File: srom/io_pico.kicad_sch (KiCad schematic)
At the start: 2 parts, among them J201 Conn_01x03_Female, U201 Pico-2 IO

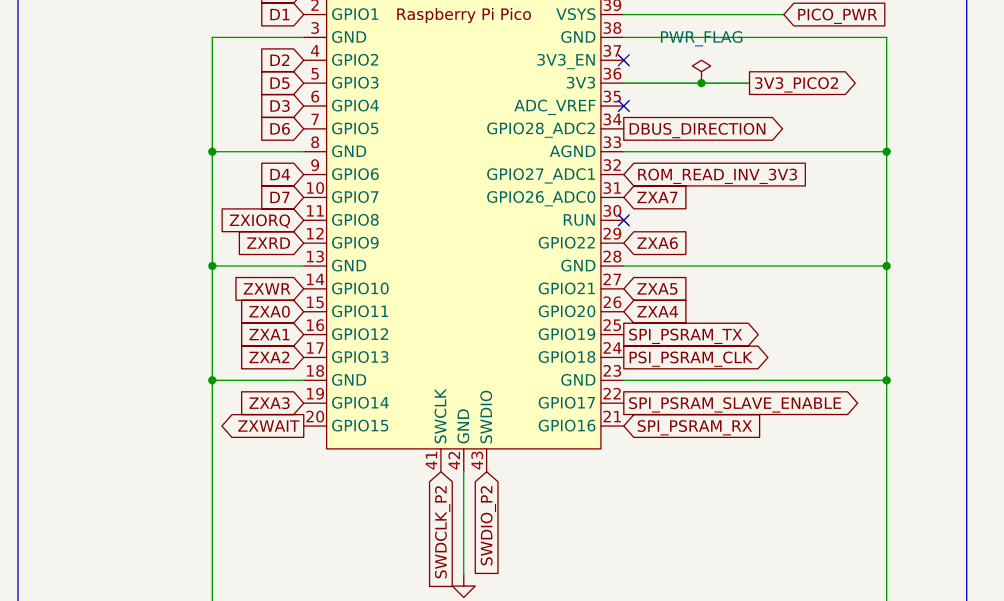
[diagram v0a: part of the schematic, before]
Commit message: code and schematic match final hardware for board #1, time to have a new one built
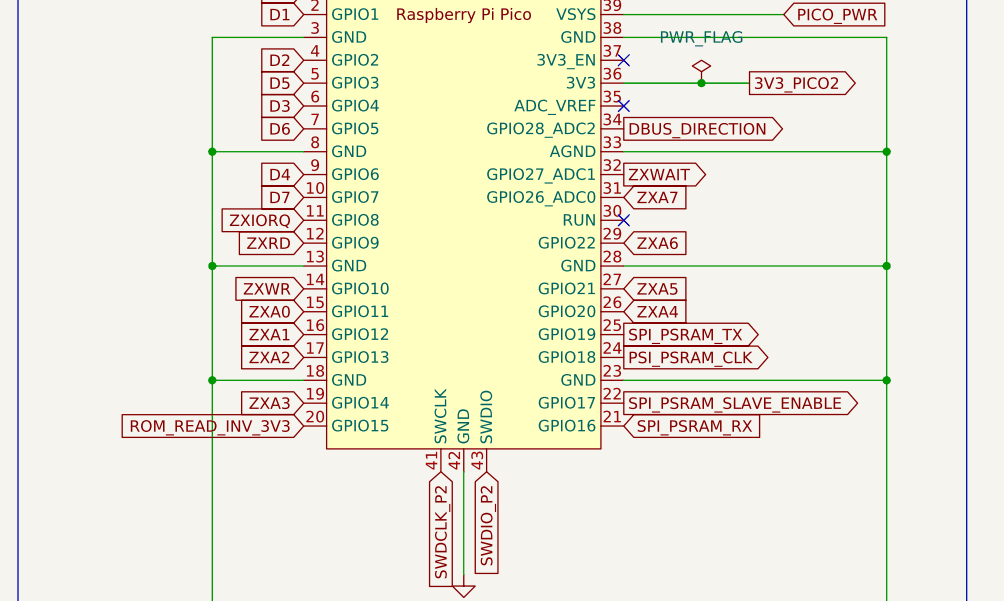
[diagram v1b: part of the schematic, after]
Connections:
- net ROM_READ_INV_3V3: now also U201.20 (GPIO15); no longer U201.32 (GPIO27_ADC1)
- net ZXWAIT: now also U201.32 (GPIO27_ADC1); no longer U201.20 (GPIO15)
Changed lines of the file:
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@@
     )
   )
-  (global_label "ZXWAIT" (shape output) (at 127 97.79 180) (fields_autoplaced)
-    (effects (font (size 1.27 1.27)) (justify right))
-    (property "Intersheet References" "${INTERSHEET_REFS}" (id 0) (at 118.0555 97.8694 0)
-      (effects (font (size 1.27 1.27)) (justify right) hide)
+  (global_label "ZXWAIT" (shape output) (at 162.56 69.85 0) (fields_autoplaced)
+    (effects (font (size 1.27 1.27)) (justify left))
+    (property "Intersheet References" "${INTERSHEET_REFS}" (id 0) (at 171.5045 69.7706 0)
+      (effects (font (size 1.27 1.27)) (justify left) hide)
     )
   )
@@
     )
   )
-  (global_label "ROM_READ_INV_3V3" (shape input) (at 162.56 69.85 0) (fields_autoplaced)
-    (effects (font (size 1.27 1.27)) (justify left))
-    (property "Intersheet References" "${INTERSHEET_REFS}" (id 0) (at 183.2369 69.7706 0)
-      (effects (font (size 1.27 1.27)) (justify left) hide)
+  (global_label "ROM_READ_INV_3V3" (shape input) (at 127 97.79 180) (fields_autoplaced)
+    (effects (font (size 1.27 1.27)) (justify right))
+    (property "Intersheet References" "${INTERSHEET_REFS}" (id 0) (at 106.3231 97.8694 0)
+      (effects (font (size 1.27 1.27)) (justify right) hide)
     )
   )

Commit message: start updating schematic for next board
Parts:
- added U202: APS6404L-3SQR_PSRAM64Mbit, Package_SO:SOIC-8_3.9x4.9mm_P1.27mm, symbol Memory_RAM:APS6404L-3SQR_PSRAM64Mbit
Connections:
- net SPI_PSRAM_SLAVE_ENABLE is gone; now on net ROM_READ_INV_3V3: U201.22 (GPIO17)
- net ZXA0 is gone; now on net ZXA3: U201.15 (GPIO11)
- net ZXA4 is gone; now on net ZXIORQ: U201.26 (GPIO20)
- net ZXA5 is gone; now on net ZXRD: U201.27 (GPIO21)
- net ZXA6 is gone; now on net ZXWR: U201.29 (GPIO22)
- net 3V3_PICO2: now also U202.8 (VCC)
- net D3: now also U201.5 (GPIO3); no longer U201.6 (GPIO4)
- net D4: now also U201.6 (GPIO4); no longer U201.9 (GPIO6)
- net D5: now also U201.7 (GPIO5); no longer U201.5 (GPIO3)
- net D6: now also U201.9 (GPIO6); no longer U201.7 (GPIO5)
- net GND: now also U202.4 (VSS)
- net ROM_READ_INV_3V3: no longer U201.20 (GPIO15)
- net ZXA3: no longer U201.19 (GPIO14)
- net ZXIORQ: no longer U201.11 (GPIO8)
- net ZXRD: no longer U201.12 (GPIO9)
- net ZXWR: no longer U201.14 (GPIO10)
- net PSI_PSRAM_CLK renamed SPI0_PSRAM_CLK
- net SPI0_PSRAM_CLK: now also U202.6 (SCLK)
- net SPI_PSRAM_RX renamed SPI0_PSRAM_MISO
- net SPI0_PSRAM_MISO: now also U202.2 (SO/SIO)
- net SPI_PSRAM_TX renamed SPI0_PSRAM_MOSI
- net SPI0_PSRAM_MOSI: now also U202.5 (SI/SIO)
- net ZXA1 renamed SPI1_UI_MOSI
- net ZXA2 renamed SPI1_UI_SLAVE_ENABLE
- net ZXA7 renamed SPI0_PSRAM_SLAVE_ENABLE
- net SPI0_PSRAM_SLAVE_ENABLE: now also U202.1 (~{CE})
- new net IF1_PORT_ACTIVE: U201.11 (GPIO8)
- new net SPI1_UI_CLK: U201.19 (GPIO14)
- new net SPI1_UI_MISO: U201.20 (GPIO15)
- no-connect marks 4 -> 8
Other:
- note added: "Pico watches the /IORQ waiting for a Z80 IN or OUT. It knows which from the /RD and /WR lines. It only needs the lower 8 bits of the address bus, and loads the result onto the data bus lines. This Pico does the data bus level shifter direction change for both a memory read and an IO read. The PIO program which changes the level shifter (BUS_DIRECTION) runs here. That's why ROM_READ_INV_3V3 is req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"
- note removed: "NOTE: I could move wait onto the ADC GPIO to save the level shift of ROM_READ_INV? Can I move the SPI SLAVE_EN, that's an output"
- note removed: "Pico watches the /IORQ waiting for a Z80 IN or OUT. It knows which from the /RD and /WR lines. It only needs the lower 8 bits of the address bus, and loads the result onto the data bus lines. This Pico does the data bus level shifter direction change for both a memory read and an IO read. The PIO program which changes the level shifter (BUS_DIRECTION) runs here. That's why ROM_READ_INV is require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"

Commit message: first draft of layout of board 2
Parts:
- added C201: C_Small, Capacitor_SMD:C_1206_3216Metric, symbol Device:C_Small
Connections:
- net 3V3_PICO2: now also C201.1
- net GND: now also C201.2
- net ZXA3: now also U201.12 (GPIO9); no longer U201.15 (GPIO11)
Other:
- note added: "External SPI-connected pseudo-DRAM. This one is an 8MB chip. 2MB will probably do, it needs to be enough to hold 8 MDR images."
- note added: "SPI0 Master, to external SRAM"
- note added: "SPI1 Slave, to UI Pico"
- moved on the sheet: U201, U202

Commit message: more work on the layout of board 2
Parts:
- added J202: Conn_01x05_Female, Connector_PinHeader_2.54mm:PinHeader_1x05_P2.54mm_Vertical, symbol Connector:Conn_01x05_Female
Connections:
- net ZXA3: now also J202.2 (Pin_2)
- net ZXIORQ: now also J202.5 (Pin_5)
- net ZXRD: now also J202.4 (Pin_4)
- net ZXWAIT: now also J202.1 (Pin_1)
- net ZXWR: now also J202.3 (Pin_3)
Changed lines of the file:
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@@
     (effects (font (size 1.27 1.27)) (justify left bottom))
   )
+  (global_label "ZXIORQ" (shape output) (at 175.26 106.426 180) (fields_autoplaced)
+    (effects (font (size 1.27 1.27)) (justify right))
+    (property "Intersheet References" "${INTERSHEET_REFS}" (id 0) (at 165.8921 106.5054 0)
+      (effects (font (size 1.27 1.27)) (justify right) hide)
+    )
+  )
+  (global_label "ZXWR" (shape output) (at 175.26 101.346 180) (fields_autoplaced)
+    (effects (font (size 1.27 1.27)) (justify right))
+    (property "Intersheet References" "${INTERSHEET_REFS}" (id 0) (at 167.7064 101.4254 0)
+      (effects (font (size 1.27 1.27)) (justify right) hide)
+    )
+  )
+  (global_label "ZXA3" (shape output) (at 175.26 98.806 180) (fields_autoplaced)
+    (effects (font (size 1.27 1.27)) (justify right))
+    (property "Intersheet References" "${INTERSHEET_REFS}" (id 0) (at 168.1298 98.7266 0)
+      (effects (font (size 1.27 1.27)) (justify right) hide)
+    )
+  )
   (global_label "SPI1_UI_MISO" (shape output) (at 56.642 79.248 180) (fields_autoplaced)
     (effects (font (size 1.27 1.27)) (justify right))
@@
     )
   )
+  (global_label "ZXRD" (shape output) (at 175.26 103.886 180) (fields_autoplaced)
+    (effects (font (size 1.27 1.27)) (justify right))
+    (property "Intersheet References" "${INTERSHEET_REFS}" (id 0) (at 167.8879 103.9654 0)
+      (effects (font (size 1.27 1.27)) (justify right) hide)
+    )
+  )
   (global_label "ZXWAIT" (shape output) (at 92.202 51.308 0) (fields_autoplaced)
     (effects (font (size 1.27 1.27)) (justify left))
@@
     (effects (font (size 1.27 1.27)) (justify right))
     (property "Intersheet References" "${INTERSHEET_REFS}" (id 0) (at 38.3841 56.3086 0)
+      (effects (font (size 1.27 1.27)) (justify right) hide)
+    )
+  )
+  (global_label "ZXWAIT" (shape output) (at 175.26 96.266 180) (fields_autoplaced)
+    (effects (font (size 1.27 1.27)) (justify right))
+    (property "Intersheet References" "${INTERSHEET_REFS}" (id 0) (at 166.3155 96.1866 0)
       (effects (font (size 1.27 1.27)) (justify right) hide)
     )
@@
     (pin "2")
   )
+  (symbol (lib_id "Connector:Conn_01x05_Female") (at 180.34 101.346 0) (unit 1)
+    (in_bom yes) (on_board yes) (fields_autoplaced)
+    (property "Reference" "J202" (id 0) (at 181.61 100.0759 0)
+      (effects (font (size 1.27 1.27)) (justify left))
+    )
+    (property "Value" "Conn_01x05_Female" (id 1) (at 181.61 102.6159 0)
+      (effects (font (size 1.27 1.27)) (justify left))
+    )
+    (property "Footprint" "Connector_PinHeader_2.54mm:PinHeader_1x05_P2.54mm_Vertical" (id 2) (at 180.34 101.346 0)
+      (effects (font (size 1.27 1.27)) hide)
+    )
+    (property "Datasheet" "~" (id 3) (at 180.34 101.346 0)
+      (effects (font (size 1.27 1.27)) hide)
+    )
+    (pin "1")
+    (pin "2")
+    (pin "3")
+    (pin "4")
+    (pin "5")
+  )
   (symbol (lib_id "pico-sym:Pico") (at 74.422 55.118 0) (unit 1)

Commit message: v1.3 of the board off to production
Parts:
- removed J202: Conn_01x05_Female, Connector_PinHeader_2.54mm:PinHeader_1x05_P2.54mm_Vertical, symbol Connector:Conn_01x05_Female
- added J202: Conn_01x06_Female, Connector_PinHeader_2.54mm:PinHeader_1x06_P2.54mm_Vertical, symbol Connector:Conn_01x06_Female
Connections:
- net ZXA3: now also J202.2 (Pin_2)
- net ZXIORQ: now also J202.5 (Pin_5)
- net ZXRD: now also J202.4 (Pin_4)
- net ZXWAIT: now also J202.1 (Pin_1)
- net ZXWR: now also J202.3 (Pin_3)
- net TEST_BLIPPER_P2: now reaches U201.14 (GPIO10)
- net TEST_BLIPPER_P2: now also J202.6 (Pin_6)
- no-connect marks 8 -> 7
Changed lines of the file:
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@@
   (no_connect (at 92.202 38.608))
   (no_connect (at 186.182 40.132))
-  (no_connect (at 56.642 64.008))
   (no_connect (at 56.642 66.548))
   (no_connect (at 92.202 56.388))
@@
     )
   )
+  (global_label "TEST_BLIPPER_P2" (shape output) (at 56.642 64.008 180) (fields_autoplaced)
+    (effects (font (size 1.27 1.27)) (justify right))
+    (property "Intersheet References" "${INTERSHEET_REFS}" (id 0) (at 37.6584 63.9286 0)
+      (effects (font (size 1.27 1.27)) (justify right) hide)
+    )
+  )
   (global_label "D1" (shape input) (at 56.642 33.528 180) (fields_autoplaced)
     (effects (font (size 1.27 1.27)) (justify right))
@@
     (property "Intersheet References" "${INTERSHEET_REFS}" (id 0) (at 110.4599 46.1486 0)
       (effects (font (size 1.27 1.27)) (justify left) hide)
+    )
+  )
+  (global_label "TEST_BLIPPER_P2" (shape output) (at 175.26 108.966 180) (fields_autoplaced)
+    (effects (font (size 1.27 1.27)) (justify right))
+    (property "Intersheet References" "${INTERSHEET_REFS}" (id 0) (at 156.2764 108.8866 0)
+      (effects (font (size 1.27 1.27)) (justify right) hide)
     )
   )
@@
     (pin "1")
   )
+  (symbol (lib_id "Connector:Conn_01x06_Female") (at 180.34 101.346 0) (unit 1)
+    (in_bom yes) (on_board yes) (fields_autoplaced)
+    (property "Reference" "J202" (id 0) (at 181.61 101.3459 0)
+      (effects (font (size 1.27 1.27)) (justify left))
+    )
+    (property "Value" "Conn_01x06_Female" (id 1) (at 181.61 103.8859 0)
+      (effects (font (size 1.27 1.27)) (justify left))
+    )
+    (property "Footprint" "Connector_PinHeader_2.54mm:PinHeader_1x06_P2.54mm_Vertical" (id 2) (at 180.34 101.346 0)
+      (effects (font (size 1.27 1.27)) hide)
+    )
+    (property "Datasheet" "~" (id 3) (at 180.34 101.346 0)
+      (effects (font (size 1.27 1.27)) hide)
+    )
+    (pin "1")
+    (pin "2")
+    (pin "3")
+    (pin "4")
+    (pin "5")
+    (pin "6")
+  )
   (symbol (lib_id "power:GND") (at 173.482 55.372 0) (unit 1)
     (in_bom yes) (on_board yes) (fields_autoplaced)
@@
     (pin "2")
   )
-  (symbol (lib_id "Connector:Conn_01x05_Female") (at 180.34 101.346 0) (unit 1)
-    (in_bom yes) (on_board yes) (fields_autoplaced)
-    (property "Reference" "J202" (id 0) (at 181.61 100.0759 0)
-      (effects (font (size 1.27 1.27)) (justify left))
-    )
-    (property "Value" "Conn_01x05_Female" (id 1) (at 181.61 102.6159 0)
-      (effects (font (size 1.27 1.27)) (justify left))
-    )
-    (property "Footprint" "Connector_PinHeader_2.54mm:PinHeader_1x05_P2.54mm_Vertical" (id 2) (at 180.34 101.346 0)
-      (effects (font (size 1.27 1.27)) hide)
-    )
-    (property "Datasheet" "~" (id 3) (at 180.34 101.346 0)
-      (effects (font (size 1.27 1.27)) hide)
-    )
-    (pin "1")
-    (pin "2")
-    (pin "3")
-    (pin "4")
-    (pin "5")
-  )
   (symbol (lib_id "pico-sym:Pico") (at 74.422 55.118 0) (unit 1)
